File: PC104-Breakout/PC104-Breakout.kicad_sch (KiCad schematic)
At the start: 9 parts, among them J1 Screw_Terminal_01x02, J2 Screw_Terminal_01x02, J3 Screw_Terminal_01x02

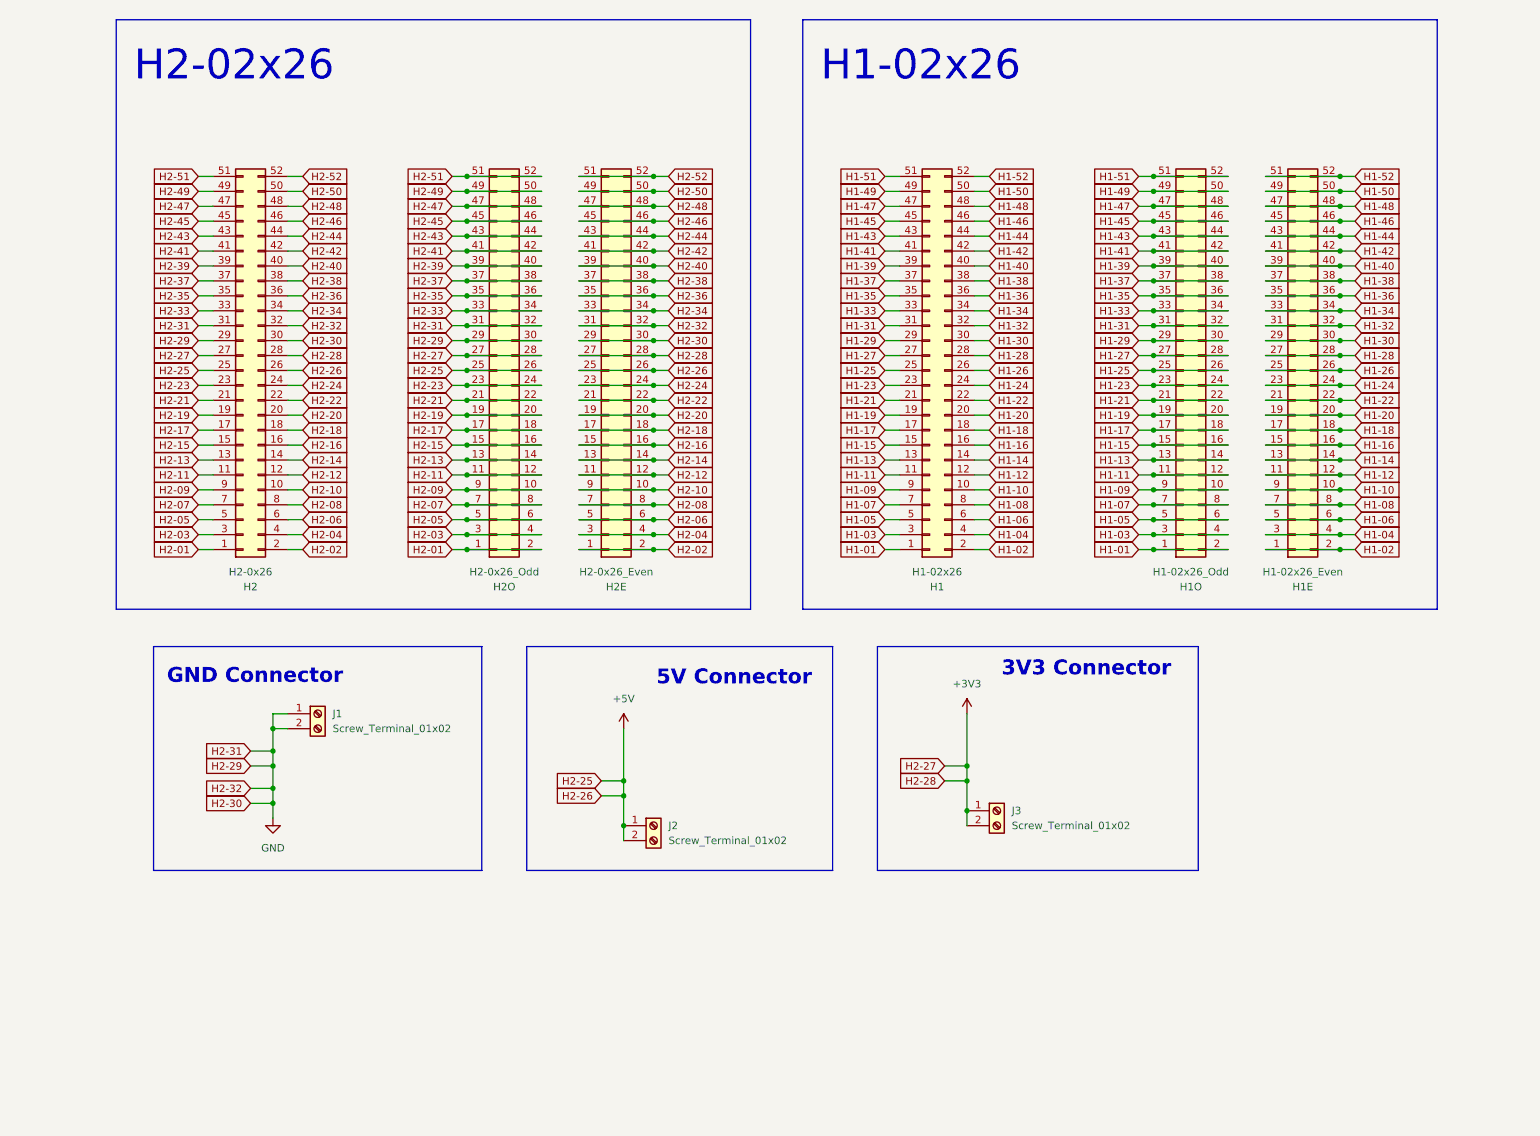
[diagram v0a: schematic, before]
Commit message: flipped headers to face correct direction
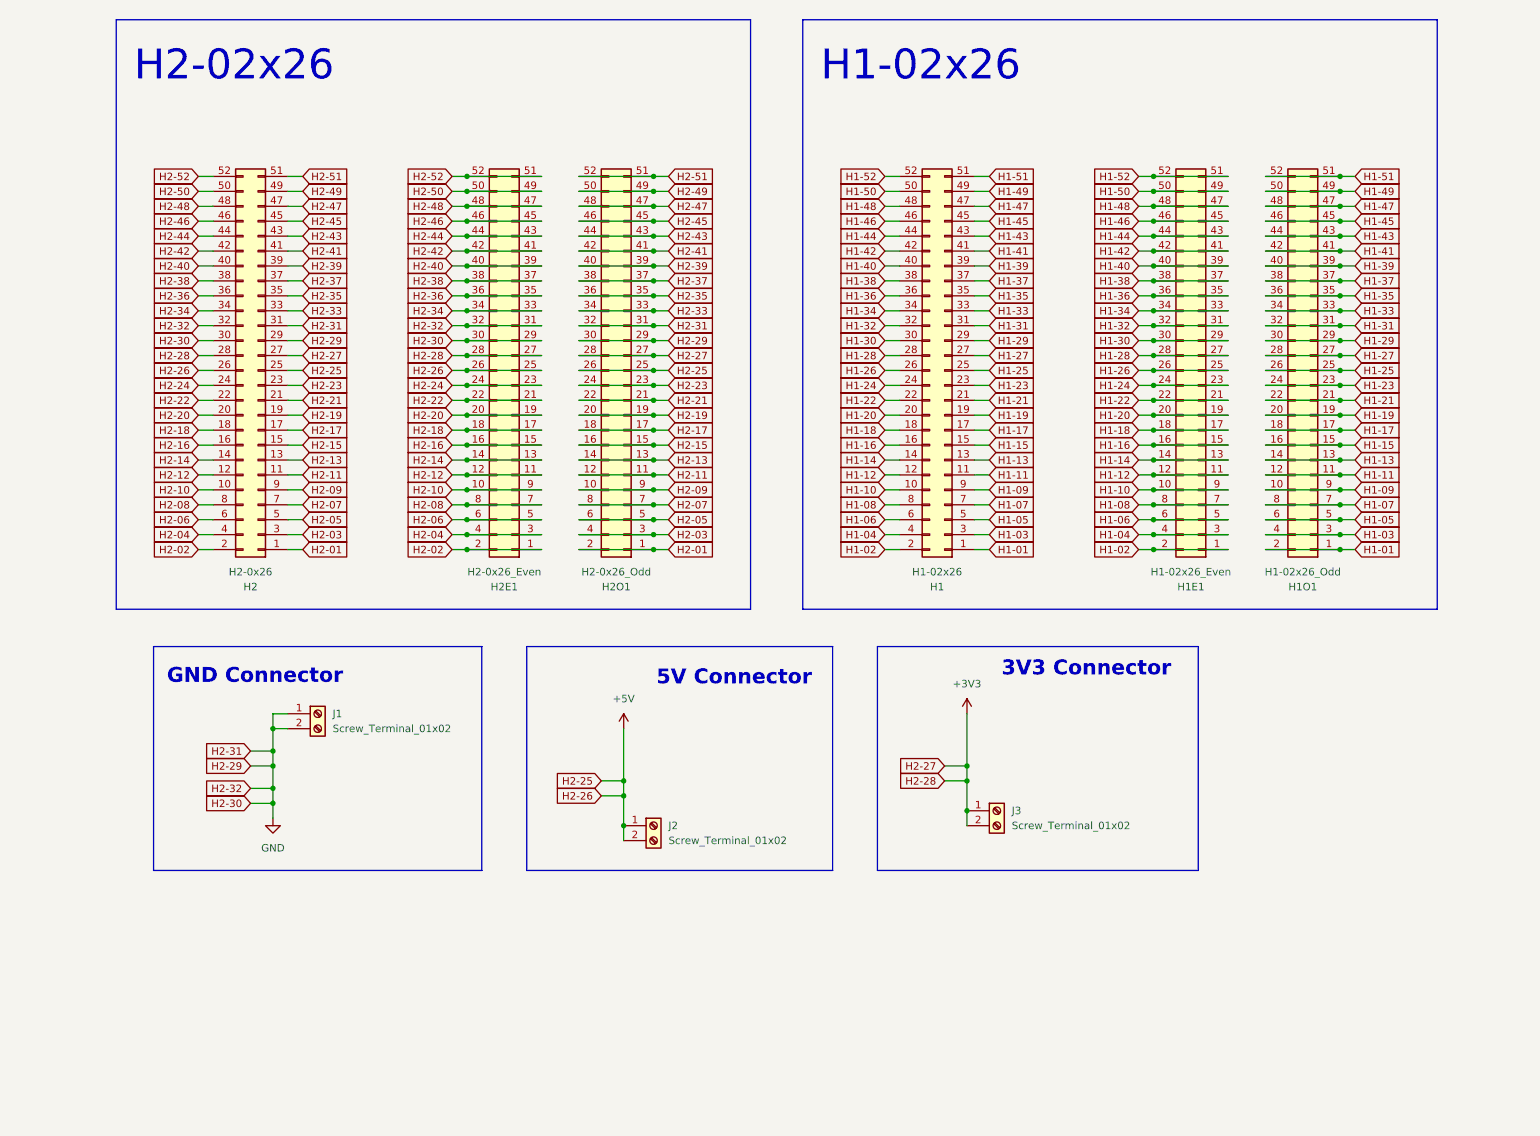
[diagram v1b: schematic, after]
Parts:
- H1, H2: footprint (none) -> Connector_PinHeader_2.54mm:PinHeader_2x26_P2.54mm_Vertical
- H1E1: renamed from H1E; footprint (none) -> Connector_PinHeader_2.54mm:PinHeader_2x26_P2.54mm_Vertical
- H1O1: renamed from H1O; footprint (none) -> Connector_PinHeader_2.54mm:PinHeader_2x26_P2.54mm_Vertical
- H2E1: renamed from H2E; footprint (none) -> Connector_PinHeader_2.54mm:PinHeader_2x26_P2.54mm_Vertical
- H2O1: renamed from H2O; footprint (none) -> Connector_PinHeader_2.54mm:PinHeader_2x26_P2.54mm_Vertical
- J1, J2, J3: footprint (none) -> TerminalBlock:TerminalBlock_bornier-2_P5.08mm
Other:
- moved on the sheet: H1, H1E1, H1O1, H2, H2E1, H2O1

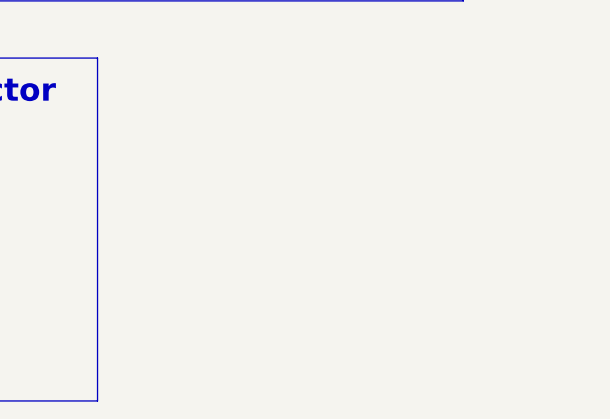
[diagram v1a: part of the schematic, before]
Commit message: added screwholes
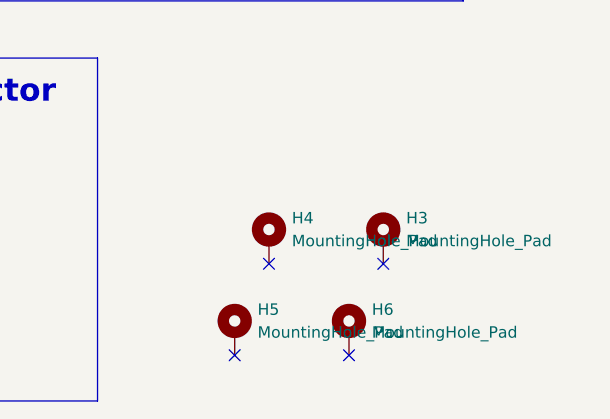
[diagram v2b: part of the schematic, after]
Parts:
- added H3, H4, H5, H6: MountingHole_Pad, MountingHole:MountingHole_3.2mm_M3_Pad, symbol Mechanical:MountingHole_Pad
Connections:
- no-connect marks 0 -> 4

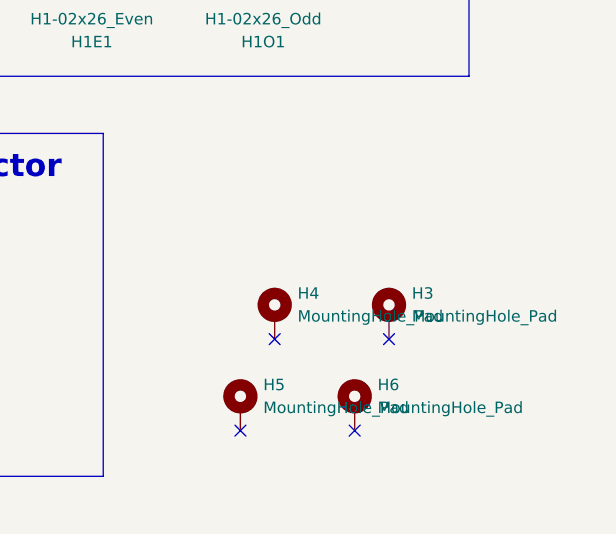
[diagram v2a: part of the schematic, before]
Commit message: Positioned external mounting holes
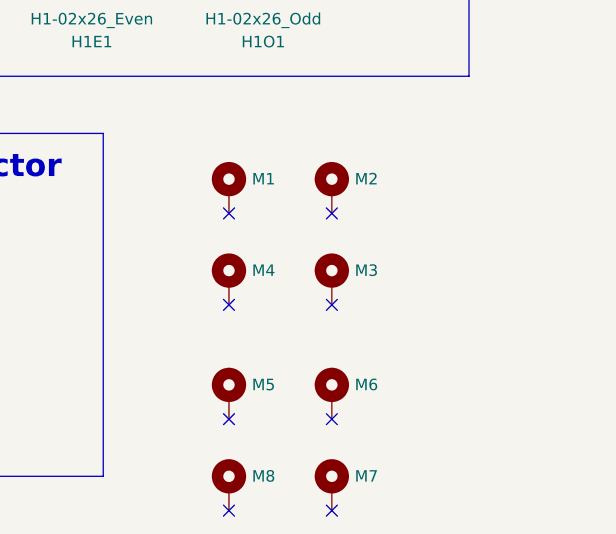
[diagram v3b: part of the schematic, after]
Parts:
- added M5, M6, M7, M8: MountingHole_Pad, MountingHole:MountingHole_3.2mm_M3_Pad, symbol Mechanical:MountingHole_Pad
- renumbered H4 to M1, H3 to M2, H6 to M3, H5 to M4
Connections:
- no-connect marks 4 -> 8
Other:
- moved on the sheet: M1, M2, M3, M4

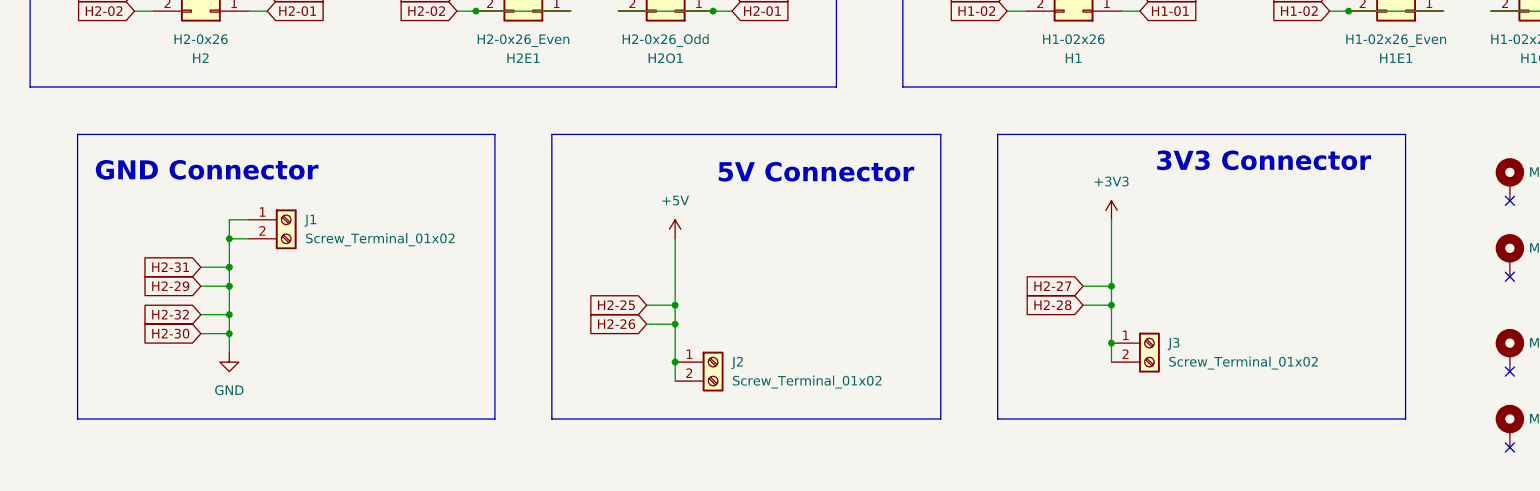
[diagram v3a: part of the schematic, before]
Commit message: Added 3.3V and GND LEDs
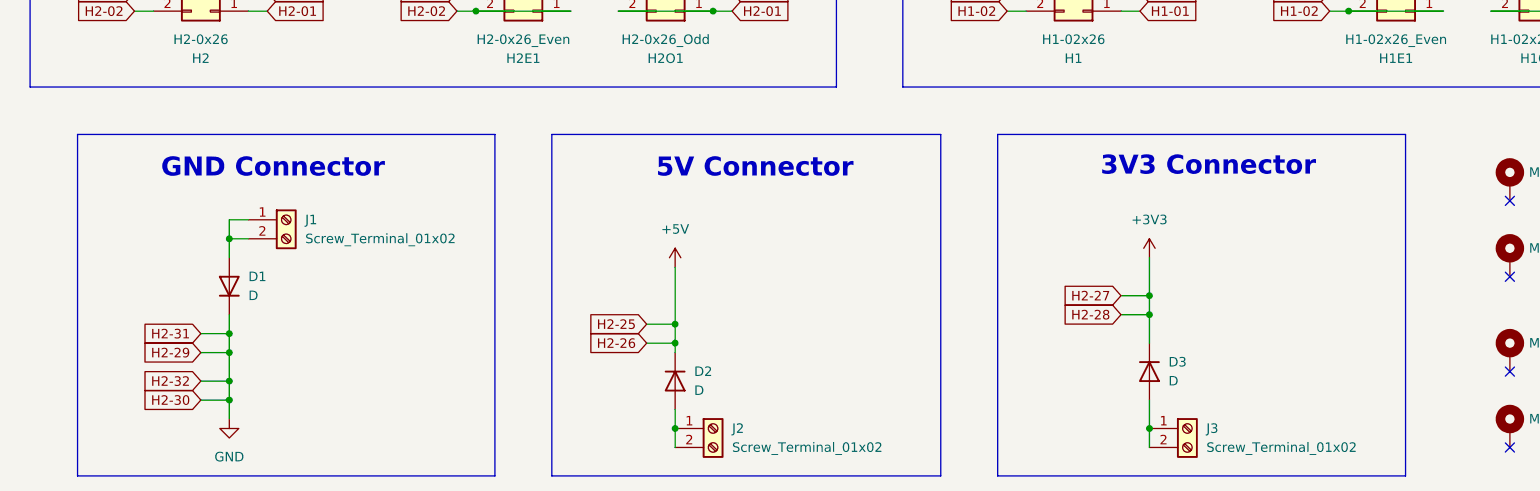
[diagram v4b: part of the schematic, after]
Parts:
- added D1, D2, D3: D, Diode_SMD:D_1206_3216Metric_Pad1.42x1.75mm_HandSolder, symbol Device:D
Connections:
- net +3V3: now also D3.1 (K); no longer J3.1 (Pin_1), J3.2 (Pin_2)
- net +5V: now also D2.1 (K); no longer J2.1 (Pin_1), J2.2 (Pin_2)
- net GND: now also D1.1 (K); no longer J1.1 (Pin_1), J1.2 (Pin_2)
- new net: D1.2 (A), J1.1 (Pin_1), J1.2 (Pin_2)
- new net: D2.2 (A), J2.1 (Pin_1), J2.2 (Pin_2)
- new net: D3.2 (A), J3.1 (Pin_1), J3.2 (Pin_2)
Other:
- moved on the sheet: J2, J3

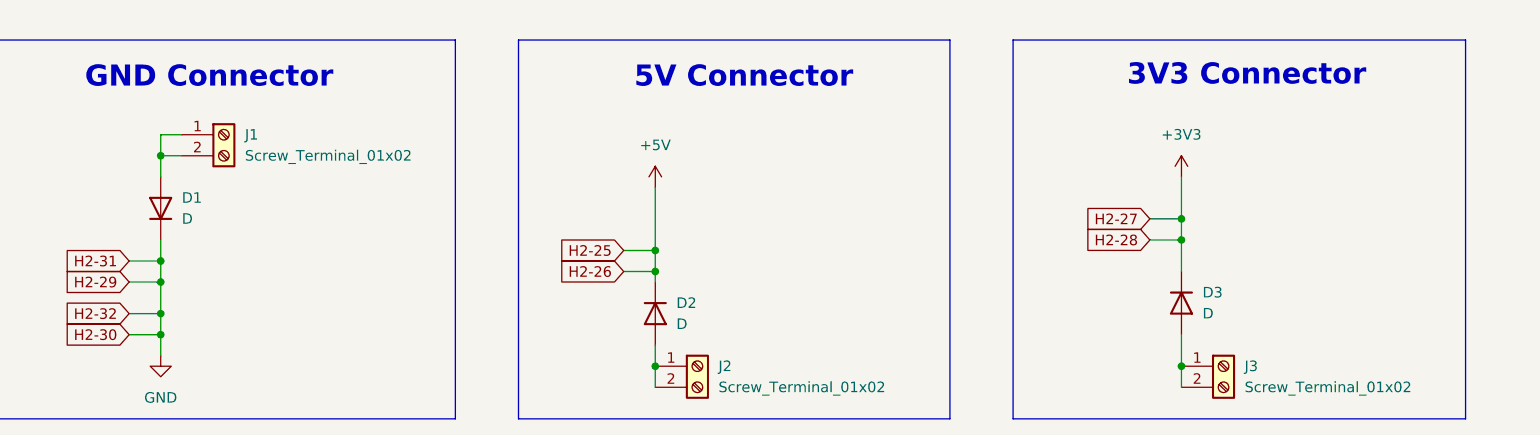
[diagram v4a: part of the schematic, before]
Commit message: Fixed LED orientations and finalized board design
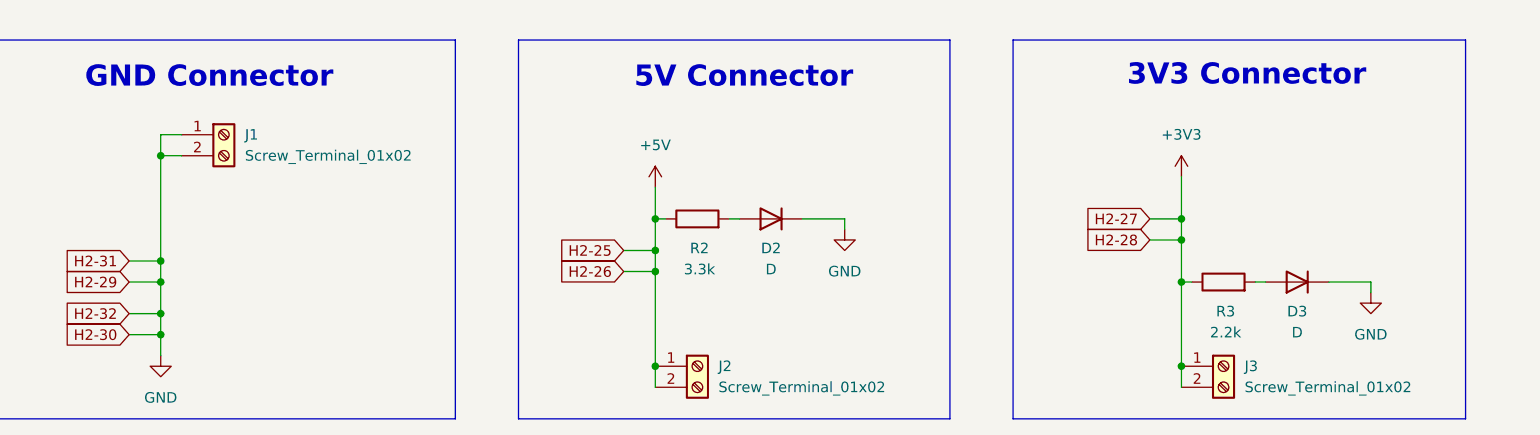
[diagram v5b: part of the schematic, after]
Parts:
- removed D1: D, Diode_SMD:D_1206_3216Metric_Pad1.42x1.75mm_HandSolder, symbol Device:D
- added R2: 3.3k, Resistor_SMD:R_1206_3216Metric_Pad1.30x1.75mm_HandSolder, symbol Device:R
- added R3: 2.2k, Resistor_SMD:R_1206_3216Metric_Pad1.30x1.75mm_HandSolder, symbol Device:R
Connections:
- net +3V3: now also J3.1 (Pin_1), J3.2 (Pin_2), R3.1; no longer D3.1 (K)
- net +5V: now also J2.1 (Pin_1), J2.2 (Pin_2), R2.1; no longer D2.1 (K)
- net GND: now also D2.1 (K), D3.1 (K), J1.1 (Pin_1), J1.2 (Pin_2)
- new net: D2.2 (A), R2.2
- new net: D3.2 (A), R3.2

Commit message: Update for Rev 3, do layout
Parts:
- removed D2, D3: D, Diode_SMD:D_1206_3216Metric_Pad1.42x1.75mm_HandSolder, symbol Device:D
- removed J1, J2, J3: Screw_Terminal_01x02, TerminalBlock:TerminalBlock_bornier-2_P5.08mm, symbol Connector:Screw_Terminal_01x02
- added D1, D2, D3, D4, D5, D6: LED, LED_SMD:LED_0603_1608Metric_Pad1.05x0.95mm_HandSolder, symbol Device:LED
- added J4, J5, J6: Screw_Terminal_01x02, TerminalBlock:TerminalBlock_bornier-2_P5.08mm, symbol Connector:Screw_Terminal_01x02
- added J7, J8, J9: Conn_01x02, Connector_PinHeader_2.54mm:PinHeader_1x03_P2.54mm_Vertical, symbol Connector_Generic:Conn_01x03
- added LG1, LG2: MountingHole, PC104-Breakout-Lib:CTS-Logo-50x25, symbol Mechanical:MountingHole
- added M10, M11, M12, M9: MountingHole_Pad, MountingHole:MountingHole_3.2mm_M3_Pad, symbol Mechanical:MountingHole_Pad
- added R1, R13, R14, R4, R5, R6, R7, R8: 10k, Resistor_SMD:R_0603_1608Metric_Pad0.98x0.95mm_HandSolder, symbol Device:R
- added R10, R9: 5k1, Resistor_SMD:R_0603_1608Metric_Pad0.98x0.95mm_HandSolder, symbol Device:R
- added R11, R12: 3k3, Resistor_SMD:R_0603_1608Metric_Pad0.98x0.95mm_HandSolder, symbol Device:R
- added TP1, TP2, TP3, TP4, TP5, TP6: TestPoint, PC104-Breakout-Lib:EdgeAlligatorConnector, symbol Connector:TestPoint
- R2: value 3.3k -> 10k; footprint Resistor_SMD:R_1206_3216Metric_Pad1.30x1.75mm_HandSolder -> Resistor_SMD:R_0603_1608Metric_Pad0.98x0.95mm_HandSolder
- R3: value 2.2k -> 10k; footprint Resistor_SMD:R_1206_3216Metric_Pad1.30x1.75mm_HandSolder -> Resistor_SMD:R_0603_1608Metric_Pad0.98x0.95mm_HandSolder
- renumbered H2 to H1, H1 to H2, H2O1 to H3, H1E1 to J1, H1O1 to J2, H2E1 to J3, M4 to M3, M3 to M4
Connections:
- net +3V3: now also J6.1 (Pin_1), J6.2 (Pin_2), J9.1 (Pin_1), J9.2 (Pin_2), J9.3 (Pin_3), R11.1, TP3.1, TP6.1; no longer H1.28 (Pin_28), J3.27 (Pin_27), J3.28 (Pin_28), R3.1
- net +5V: now also J5.1 (Pin_1), J5.2 (Pin_2), J8.1 (Pin_1), J8.2 (Pin_2), J8.3 (Pin_3), R9.1, TP2.1, TP5.1; no longer H1.26 (Pin_26), J3.25 (Pin_25), J3.26 (Pin_26), R2.1
- net GND: now also R2.2, R3.2, D1.1 (K), D2.1 (K), D3.1 (K), D4.1 (K), D5.1 (K), D6.1 (K), J4.1 (Pin_1), J4.2 (Pin_2), J7.1 (Pin_1), J7.2 (Pin_2), J7.3 (Pin_3), R1.2, R4.2, R5.2, R6.2, R7.2, R8.2, TP1.1, TP4.1; no longer H1.30 (Pin_30), H1.31 (Pin_31), H1.32 (Pin_32), H3.31 (Pin_31), H3.32 (Pin_32), J3.29 (Pin_29), J3.30 (Pin_30), J3.31 (Pin_31), J3.32 (Pin_32)
- net H2-45: now also R13.1
- net H2-46: now also R14.1
- net at M8.1: now also R4.1
- net at M5.1: now also R1.1
- net at M7.1: now also R3.1
- net at M6.1: now also R2.1
- new net: D1.2 (A), R9.2
- new net: M12.1, R8.1
- new net: D3.2 (A), R11.2
- new net: D4.2 (A), R12.2
- new net: M9.1, R5.1
- new net: D2.2 (A), R10.2
- new net: M11.1, R7.1
- new net: M10.1, R6.1
- new net: D5.2 (A), R13.2
- new net: D6.2 (A), R14.2
- new net H2-26: H1.26 (Pin_26), J3.25 (Pin_25), J3.26 (Pin_26), R10.1
- new net H2-28: H1.28 (Pin_28), J3.27 (Pin_27), J3.28 (Pin_28), R12.1
- new net H2-30: H1.30 (Pin_30), J3.29 (Pin_29), J3.30 (Pin_30)
- new net H2-31: H1.31 (Pin_31), H3.31 (Pin_31), H3.32 (Pin_32)
- new net H2-32: H1.32 (Pin_32), J3.31 (Pin_31), J3.32 (Pin_32)
- no-connect marks 8 -> 4
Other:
- note added: "3V3"
- note added: "5V"
- note added: "H1"
- note added: "H1-Even"
- note added: "H1-Odd"
- note added: "H2"
- note added: "H2-Even"
- note added: "H2-Odd"
- note added: "Inner Corner Holes"
- note added: "Logo"
- note added: "Main PC104 Stack Header"
- note added: "Outer Corner Holes"
- note added: "PC104 Stack Holes"
- note added: "Stack Header Breakouts"
- note added: "Vbatt"
- note added: "Voltage Breakout Points"
- note added: "Voltage Indicator LEDs"
- note removed: "3V3 Connector"
- note removed: "5V Connector"
- note removed: "GND Connector"
- note removed: "H1-02x26"
- note removed: "H2-02x26"
- moved on the sheet: H1, H2, H3, J1, J2, J3, M1, M2, M3, M4, M5, M6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
